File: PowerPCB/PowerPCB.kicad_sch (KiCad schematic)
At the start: 0 parts

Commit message: Begin PowerPCB schematic
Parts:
- added C1, C3: 10uF, symbol Device:C
- added C2: 0.1uF, symbol Device:C
- added R1: 100k, symbol Device:R_US
- added R2: 36.1k, symbol Device:R_US
- added R3: 169k, symbol Device:R_US
- added U1: TPS56637RPAR, symbol KiCad_TitoSync_Symbols:TPS56637RPAR
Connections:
- new net: R2.2, R3.1, U1.1 (EN)
- new net: R3.2, U1.8 (VIN)
- new net: R1.1, U1.4 (PG)
- new net AGND: R2.1, U1.10 (MODE), U1.3 (AGND)
- new net PGND: C1.2, C2.2, C3.2, U1.9 (PGND)
- new net VCC: R1.2

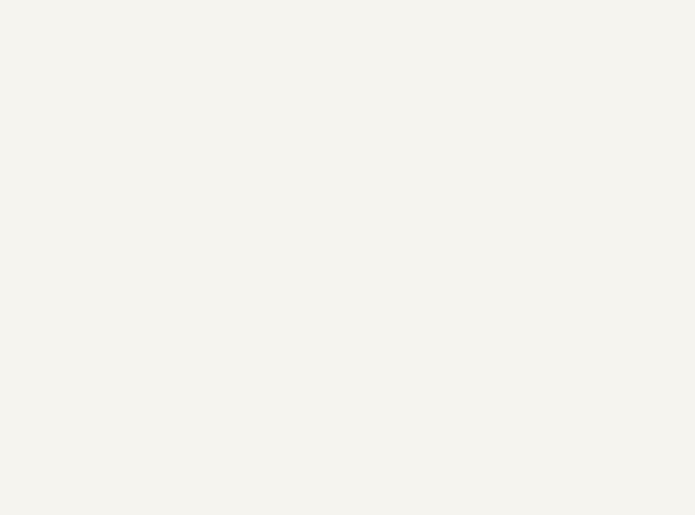
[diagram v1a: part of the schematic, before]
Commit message: Asignar footprints a símbolo fs1003
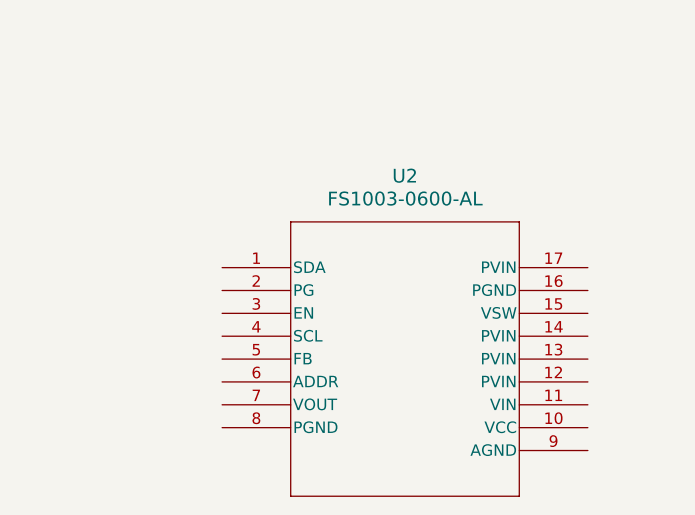
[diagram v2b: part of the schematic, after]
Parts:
- added U2: FS1003-0600-AL, Kicad_TitoSync_Footprints:fs1003-0600-al, symbol KiCad_TitoSync_Symbols:FS1003-0600-AL
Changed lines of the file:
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@@
+	)
+	(symbol
+		(lib_id "KiCad_TitoSync_Symbols:FS1003-0600-AL")
+		(at 87.63 100.33 0)
+		(unit 1)
+		(exclude_from_sim no)
+		(in_bom yes)
+		(on_board yes)
+		(dnp no)
+		(fields_autoplaced yes)
+		(property "Reference" "U2"
+			(at 107.95 90.17 0)
+			(effects
+				(font
+					(size 1.524 1.524)
+				)
+			)
+		)
+		(property "Value" "FS1003-0600-AL"
+			(at 107.95 92.71 0)
+			(effects
+				(font
+					(size 1.524 1.524)
+				)
+			)
+		)
+		(property "Footprint" "Kicad_TitoSync_Footprints:fs1003-0600-al"
+			(at 87.63 100.33 0)
+			(effects
+				(font
+					(size 1.27 1.27)
+					(italic yes)
+				)
+				(hide yes)
+			)
+		)
+		(property "Datasheet" "FS1003-0600-AL"
+			(at 87.63 100.33 0)
+			(effects
+				(font
+					(size 1.27 1.27)
+					(italic yes)
+				)
+				(hide yes)
+			)
+		)
+		(property "Description" ""
+			(at 87.63 100.33 0)
+			(effects
+				(font
+					(size 1.27 1.27)
+				)
+				(hide yes)
+			)
+		)
+		(pin "2"
+		)
+		(pin "16"
+		)
+		(pin "7"
+		)
+		(pin "1"
+		)
+		(pin "8"
+		)
+		(pin "17"
+		)
+		(pin "3"
+		)
+		(pin "4"
+		)
+		(pin "5"
+		)
+		(pin "6"
+		)
+		(pin "12"
+		)
+		(pin "13"
+		)
+		(pin "10"
+		)
+		(pin "9"
+		)
+		(pin "11"
+		)
+		(pin "15"
+		)
+		(pin "14"
+		)
+		(instances
+			(project ""
+				(path "/b4fe13f3-f661-4394-8ef5-4db29a2b0a31"
+					(reference "U2")
+					(unit 1)
+				)
+			)
+		)
 	)
 	(symbol

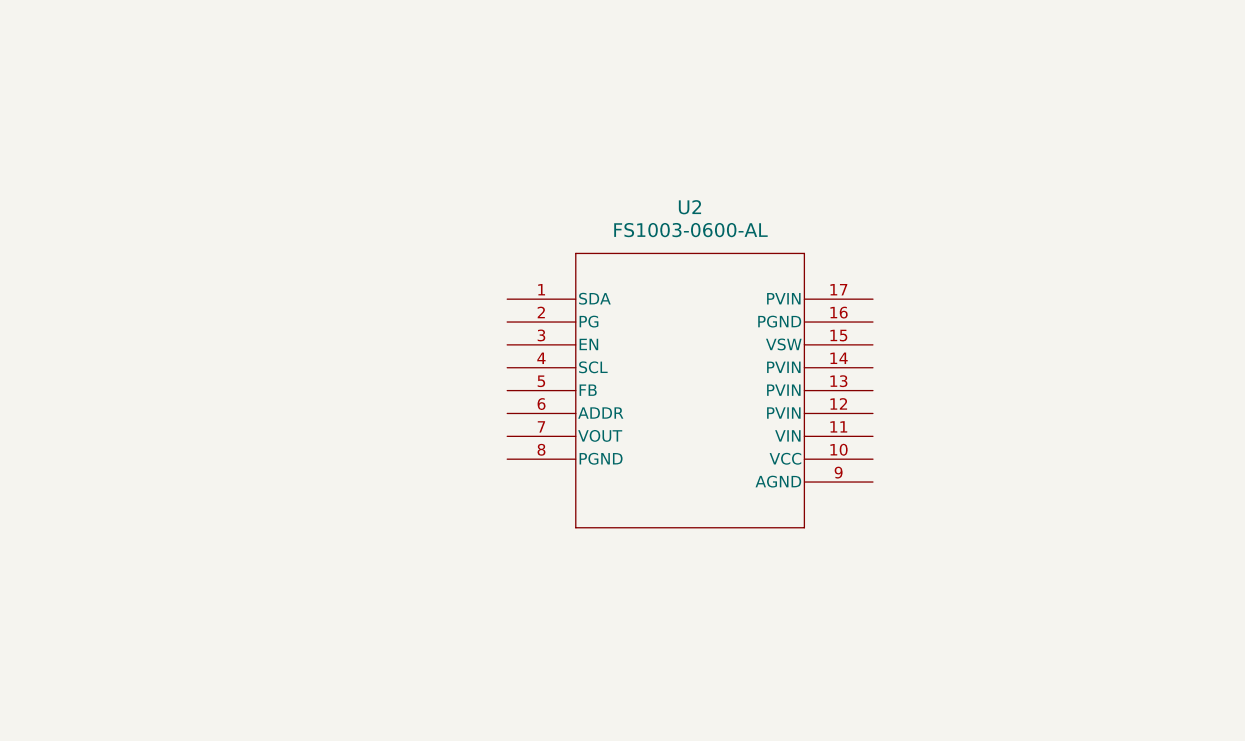
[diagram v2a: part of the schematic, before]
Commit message: Circuito 12 a 5 faltan valores
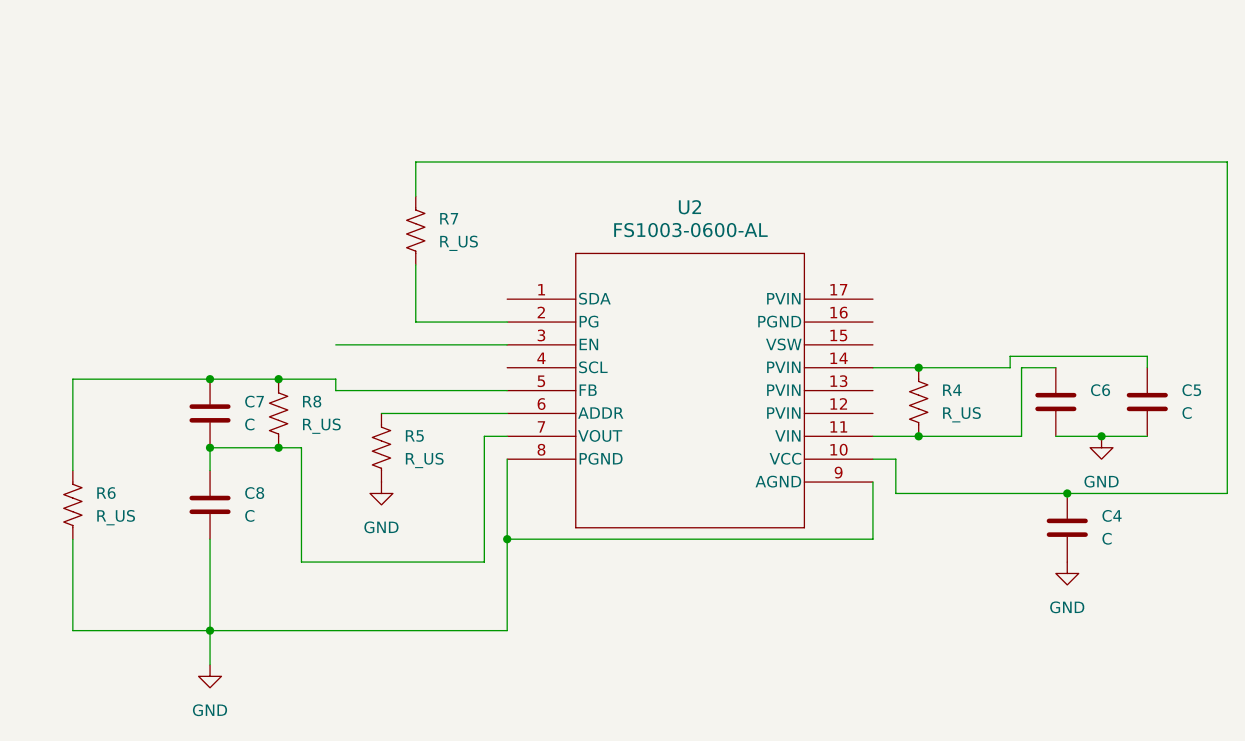
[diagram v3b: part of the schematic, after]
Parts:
- added C4, C5, C6, C7, C8: C, symbol Device:C
- added R4, R5, R6, R7, R8: R_US, symbol Device:R_US
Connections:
- net at U2.10 (VCC): now also C4.1, R7.1
- net at U2.11 (VIN): now also C6.1, R4.2
- net at U2.14 (PVIN): now also C5.1, R4.1
- net at U2.2 (PG): now also R7.2
- net at U2.5 (FB): now also C7.1, R6.1, R8.1
- net at U2.6 (ADDR): now also R5.1
- net at U2.7 (VOUT): now also C7.2, C8.1, R8.2
- net GND: now reaches U2.8 (PGND)
- net GND: now also U2.9 (AGND), C4.2, C5.2, C6.2, C8.2, R5.2, R6.2

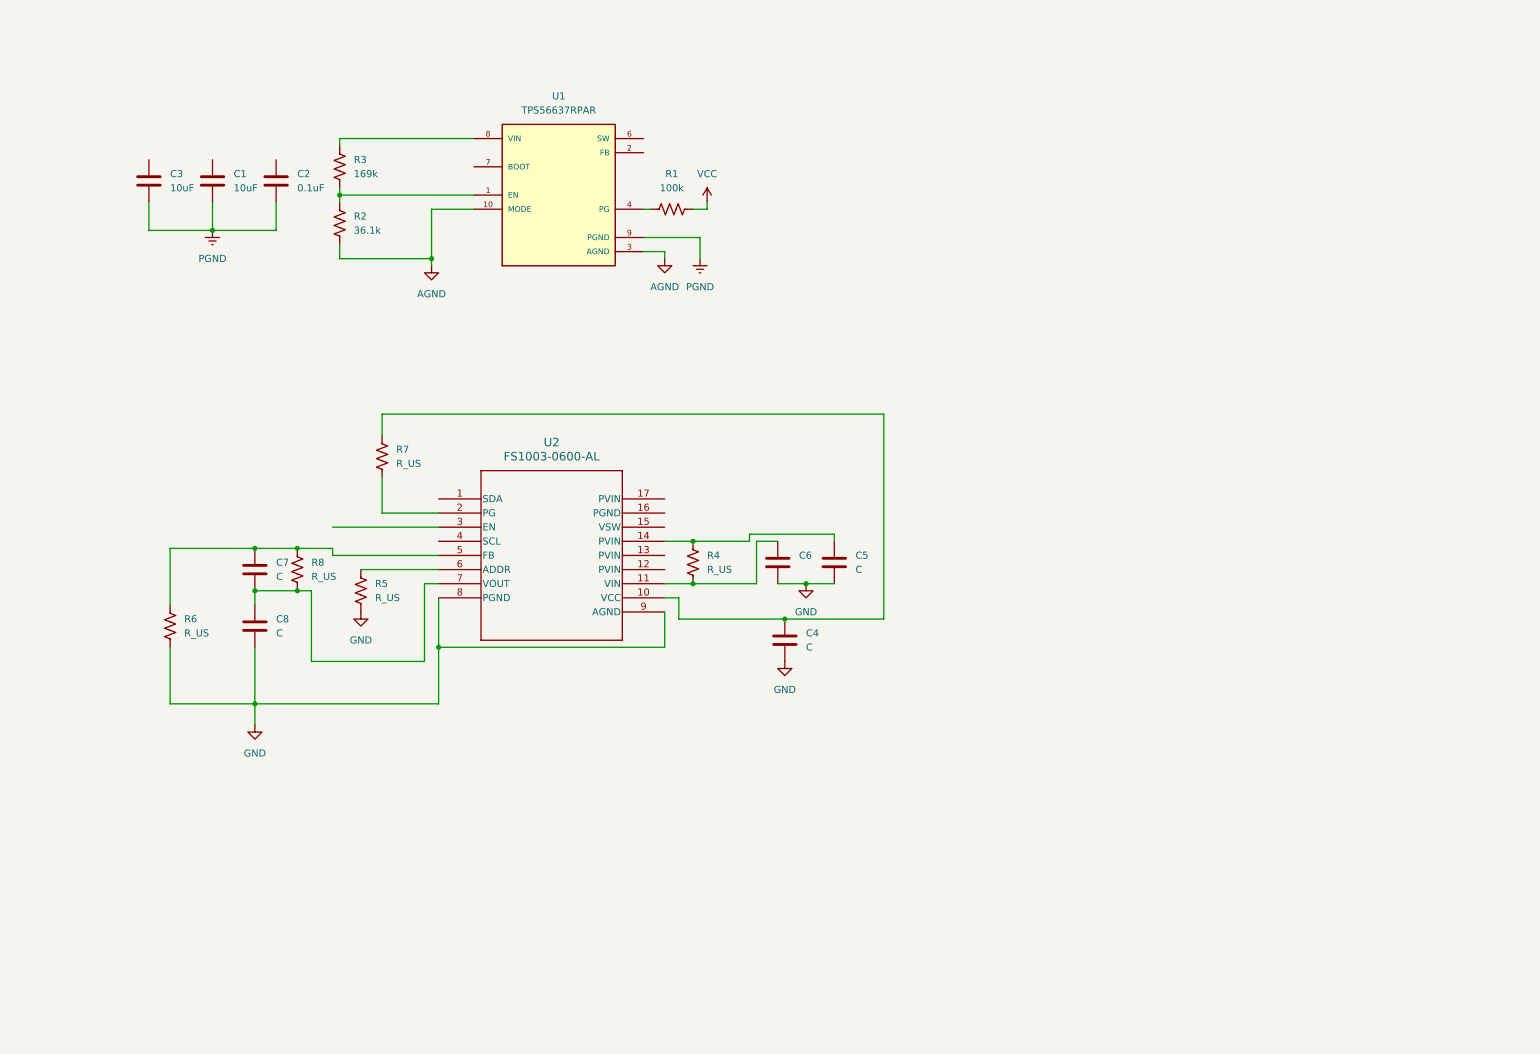
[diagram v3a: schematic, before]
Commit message: 12 V circuit complete
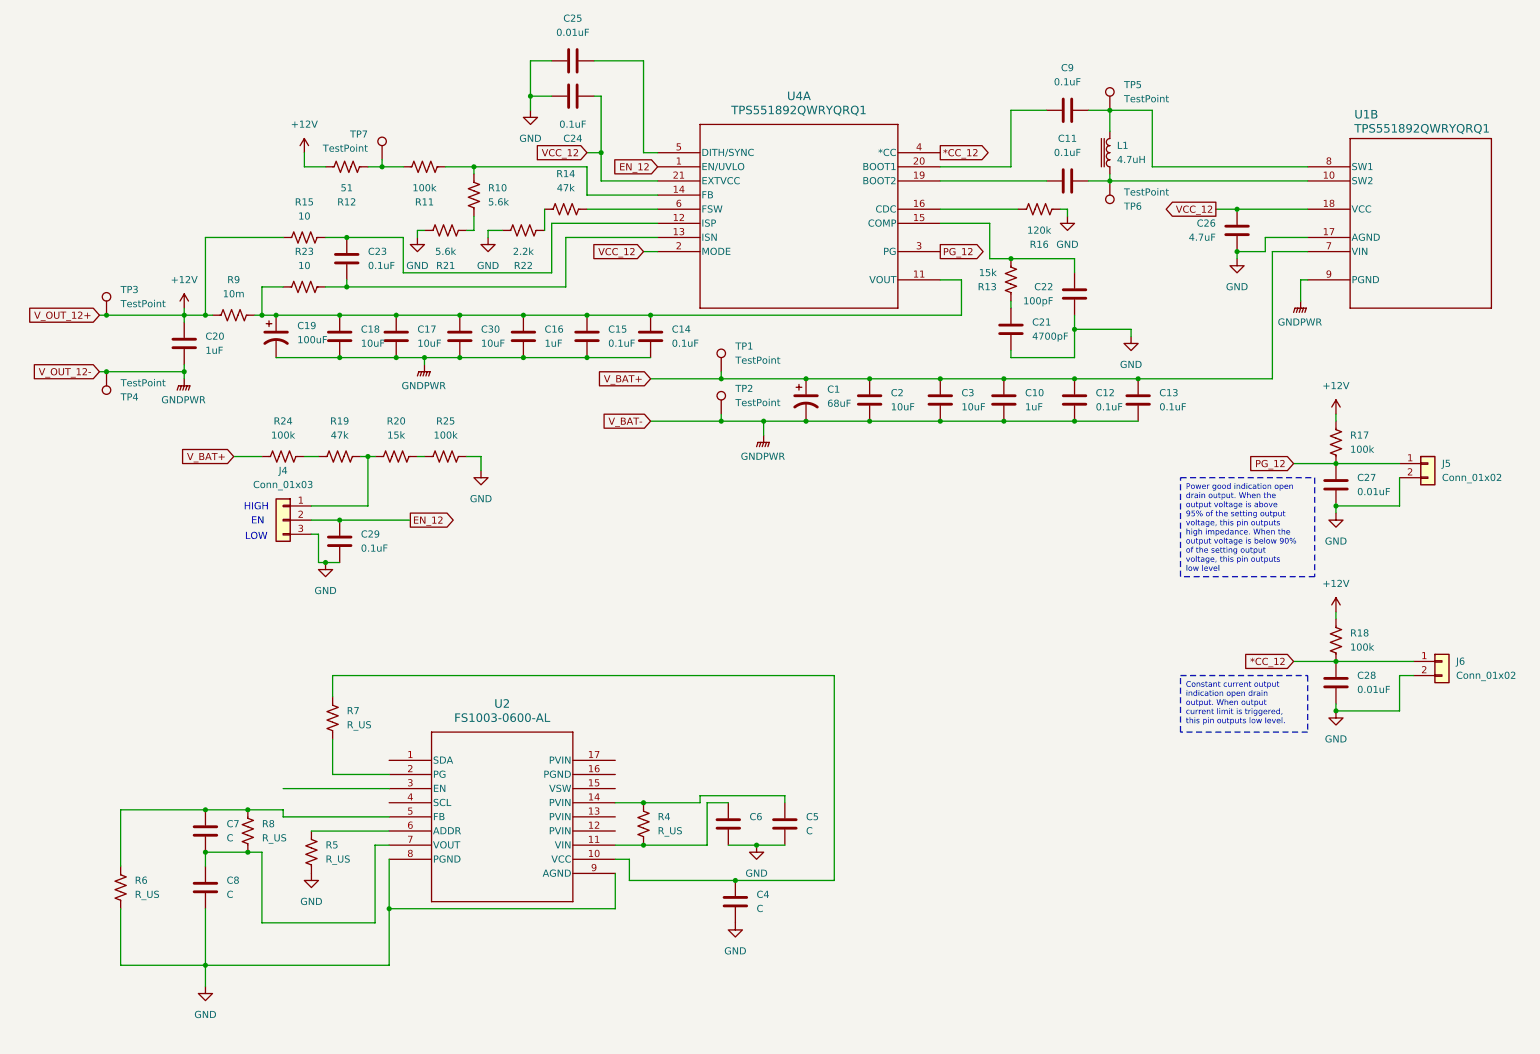
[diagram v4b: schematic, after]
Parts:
- removed C1: 10uF, symbol Device:C
- removed R1: 100k, symbol Device:R_US
- removed R2: 36.1k, symbol Device:R_US
- removed R3: 169k, symbol Device:R_US
- removed U1: TPS56637RPAR, symbol KiCad_TitoSync_Symbols:TPS56637RPAR
- added C1: 68uF, Capacitor_SMD:CP_Elec_8x10, symbol Device:C_Polarized_US
- added C10, C16, C20: 1uF, Capacitor_SMD:C_1206_3216Metric_Pad1.33x1.80mm_HandSolder, symbol Device:C
- added C11, C12, C13, C14, C15, C23, C24, C29, C9: 0.1uF, Capacitor_SMD:C_1206_3216Metric_Pad1.33x1.80mm_HandSolder, symbol Device:C
- added C17, C18, C30: 10uF, Capacitor_SMD:C_0805_2012Metric_Pad1.18x1.45mm_HandSolder, symbol Device:C
- added C19: 100uF, Capacitor_SMD:CP_Elec_6.3x5.4, symbol Device:C_Polarized_US
- added C21: 4700pF, Capacitor_SMD:C_1206_3216Metric_Pad1.33x1.80mm_HandSolder, symbol Device:C
- added C22: 100pF, Capacitor_SMD:C_0805_2012Metric_Pad1.18x1.45mm_HandSolder, symbol Device:C
- added C25, C27, C28: 0.01uF, Capacitor_SMD:C_0805_2012Metric_Pad1.18x1.45mm_HandSolder, symbol Device:C
- added C26: 4.7uF, Capacitor_SMD:C_1206_3216Metric_Pad1.33x1.80mm_HandSolder, symbol Device:C
- added J4: Conn_01x03, Connector_PinHeader_2.54mm:PinHeader_1x03_P2.54mm_Vertical, symbol Connector_Generic:Conn_01x03
- added J5, J6: Conn_01x02, Connector_PinHeader_2.54mm:PinHeader_1x02_P2.54mm_Vertical, symbol Connector_Generic:Conn_01x02
- added L1: 4.7uH, Inductor_SMD:L_Coilcraft_XAL7070-XXX, symbol Device:L_Iron
- added R10, R21: 5.6k, Resistor_SMD:R_1206_3216Metric_Pad1.30x1.75mm_HandSolder, symbol Device:R_US
- added R11, R17, R18, R24, R25: 100k, Resistor_SMD:R_0805_2012Metric_Pad1.20x1.40mm_HandSolder, symbol Device:R_US
- added R12: 51, Resistor_SMD:R_0805_2012Metric_Pad1.20x1.40mm_HandSolder, symbol Device:R_US
- added R13, R20: 15k, Resistor_SMD:R_0805_2012Metric_Pad1.20x1.40mm_HandSolder, symbol Device:R_US
- added R14, R19: 47k, Resistor_SMD:R_0805_2012Metric_Pad1.20x1.40mm_HandSolder, symbol Device:R_US
- added R15, R23: 10, Resistor_SMD:R_0805_2012Metric_Pad1.20x1.40mm_HandSolder, symbol Device:R_US
- added R16: 120k, Resistor_SMD:R_0805_2012Metric_Pad1.20x1.40mm_HandSolder, symbol Device:R_US
- added R22: 2.2k, Resistor_SMD:R_0805_2012Metric_Pad1.20x1.40mm_HandSolder, symbol Device:R_US
- added R9: 10m, Resistor_SMD:R_1206_3216Metric_Pad1.30x1.75mm_HandSolder, symbol Device:R_US
- added TP1, TP2, TP3, TP4, TP5, TP6, TP7: TestPoint, symbol Connector:TestPoint
- added U1, U4: TPS551892QWRYQRQ1, Kicad_TitoSync_Footprints:VQFN21_RYQ_TEX, symbol KiCad_TitoSync_Symbols:TPS551892QWRYQRQ1
- C2: value 0.1uF -> 10uF; footprint (none) -> Capacitor_SMD:C_0805_2012Metric_Pad1.18x1.45mm_HandSolder
- C3: footprint (none) -> Capacitor_SMD:C_0805_2012Metric_Pad1.18x1.45mm_HandSolder
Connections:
- net GND: now also C21.2, C22.2, C24.1, C25.1, C26.2, C27.2, C28.2, C29.2, J4.3 (Pin_3), J5.2 (Pin_2), J6.2 (Pin_2), R16.2, R21.1, R22.1, R25.2, U1.17 (AGND)
- net V_BAT+: now reaches C3.1
- net V_BAT+: now also C2.1, C1.1, C10.1, C12.1, C13.1, R24.1, TP1.1, U1.7 (VIN)
- net PGND renamed GNDPWR
- net GNDPWR: now also C1.2, C10.2, C12.2, C13.2, C14.2, C15.2, C16.2, C17.2, C18.2, C19.2, C20.2, C30.2, TP2.1, TP4.1, U1.9 (PGND)
- new net: R19.1, R24.2
- new net: J4.1 (Pin_1), R19.2, R20.1
- new net: C14.1, C15.1, C16.1, C17.1, C18.1, C19.1, C30.1, R23.1, R9.2, U4.11 (VOUT)
- new net: R11.1, R12.2, TP7.1
- new net: C9.1, U4.20 (BOOT1)
- new net: C9.2, L1.2, TP5.1, U1.8 (SW1)
- new net: R16.1, U4.16 (CDC)
- new net: R10.1, R21.2
- new net: R20.2, R25.1
- new net: R14.1, U4.6 (FSW)
- new net: R14.2, R22.2
- new net: C11.2, L1.1, TP6.1, U1.10 (SW2)
- new net: R10.2, R11.2, U4.14 (FB)
- new net: C21.1, R13.1
- new net: C23.2, R23.2, U4.13 (ISN)
- new net: C22.1, R13.2, U4.15 (COMP)
- new net: C23.1, R15.2, U4.12 (ISP)
- new net: C11.1, U4.19 (BOOT2)
- new net: C25.2, U4.5 (DITH/SYNC)
- new net *CC_12: C28.1, J6.1 (Pin_1), R18.2, U4.4 (*CC)
- new net +12V: C20.1, R12.1, R15.1, R17.1, R18.1, R9.1, TP3.1
- new net EN_12: C29.1, J4.2 (Pin_2), U4.1 (EN/UVLO)
- new net PG_12: C27.1, J5.1 (Pin_1), R17.2, U4.3 (PG)
- new net VCC_12: C24.2, C26.1, U1.18 (VCC), U4.2 (MODE), U4.21 (EXTVCC)
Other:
- note added: "EN"
- note added: "HIGH"
- note added: "LOW"
- moved on the sheet: C4, C5, C6, C7, C8, R4, R5, R6, R7, R8, U2

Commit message: circuito terminado
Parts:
- removed C6: C, symbol Device:C
- added Cin2, Cout2: 22u, symbol Device:C
- added Cvin: 1u, symbol Device:C
- Cff: renamed from C7; value C -> 680p
- Cin: renamed from C5; value C -> 22u
- Cout1: renamed from C8; value C -> 22u
- Cvcc: renamed from C4; value C -> C2.2u
- R4: value R_US -> 2.7
- R5: value R_US -> 0
- R7: value R_US -> 49.9
- Rbottom: renamed from R6; value R_US -> 562
- Rtop: renamed from R8; value R_US -> 4.12K
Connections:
- net GND: now also Cin2.2, Cout2.2, Cvin.2
- net at R4.2, U2.11 (VIN): now also Cvin.1
- net Vout(5V): now reaches Cff.2, Cout1.1, Rtop.2, U2.7 (VOUT)
- net Vout(5V): now also Cout2.1
- net PVin(12V): now reaches Cin.1, R4.1, U2.14 (PVIN)
- net PVin(12V): now also Cin2.1
- net En: now reaches U2.3 (EN)
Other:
- moved on the sheet: Cff, Cout1, Rbottom
